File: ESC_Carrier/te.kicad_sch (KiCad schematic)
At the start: 1 part, among them J1 TE 8-5530843-3

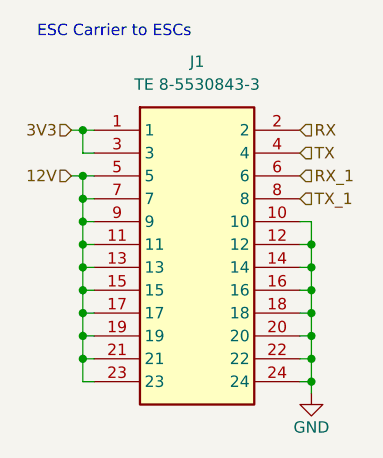
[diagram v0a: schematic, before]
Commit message: Fix: updated esc carrier to esc connectors
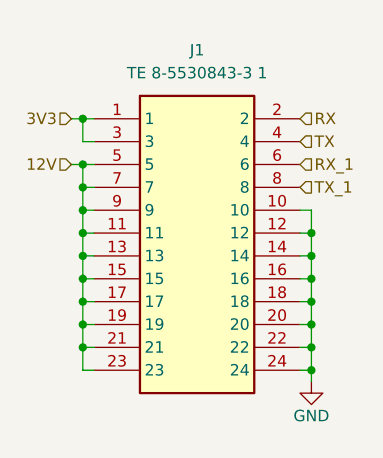
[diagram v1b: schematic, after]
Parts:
- J1: value TE 8-5530843-3 -> TE 8-5530843-3 1; footprint 855308433 -> 8-5530843-3:8-5530843-3
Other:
- note removed: "ESC Carrier to ESCs"

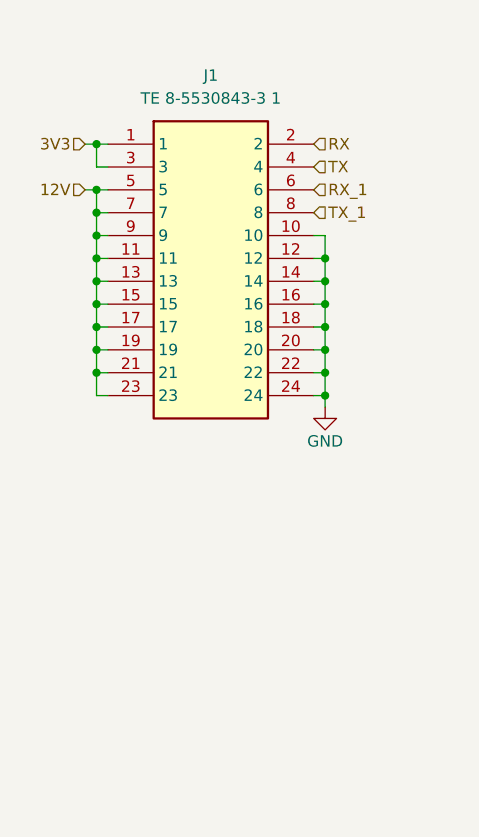
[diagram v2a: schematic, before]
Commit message: Fix: added phases to esc to esc carrier connector
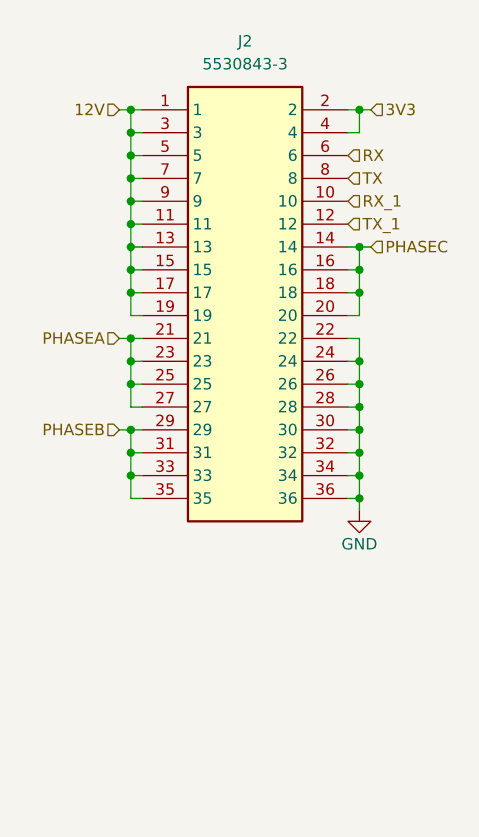
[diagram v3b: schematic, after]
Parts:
- removed J1: TE 8-5530843-3 1, 8-5530843-3:8-5530843-3, symbol 8-5530843-3:8-5530843-3
- added J2: 5530843-3, RHDR36W89P485X254_2X18_5232X928X1549P, symbol 5530843-3:5530843-3
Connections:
- net 12V: now also J2.1, J2.11, J2.13, J2.15, J2.17, J2.19, J2.3, J2.5, J2.7, J2.9
- net 3V3: now also J2.2, J2.4
- net GND: now also J2.22, J2.24, J2.26, J2.28, J2.30, J2.32, J2.34, J2.36
- net RX: now also J2.6
- net RX_1: now also J2.10
- net TX: now also J2.8
- net TX_1: now also J2.12
- new net PHASEA: J2.21, J2.23, J2.25, J2.27
- new net PHASEB: J2.29, J2.31, J2.33, J2.35
- new net PHASEC: J2.14, J2.16, J2.18, J2.20

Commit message: Feat: updated esc to esc carrier connector, updated test points
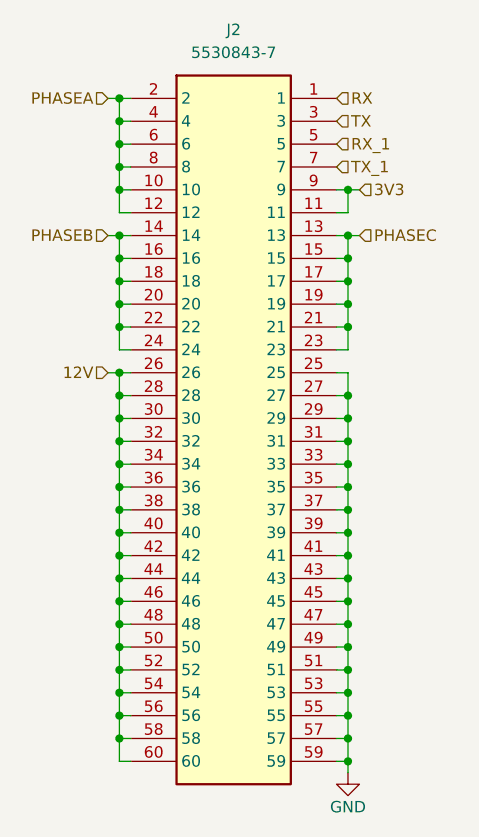
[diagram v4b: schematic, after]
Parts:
- removed J2: 5530843-3, RHDR36W89P485X254_2X18_5232X928X1549P, symbol 5530843-3:5530843-3
- added J2: 5530843-7, 55308437, symbol 5530843-7:5530843-7
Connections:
- net 12V: now also J2.26, J2.28, J2.30, J2.32, J2.34, J2.36, J2.38, J2.40, J2.42, J2.44, J2.46, J2.48, J2.50, J2.52, J2.54, J2.56, J2.58, J2.60
- net 3V3: now also J2.11, J2.9
- net GND: now also J2.25, J2.27, J2.29, J2.31, J2.33, J2.35, J2.37, J2.39, J2.41, J2.43, J2.45, J2.47, J2.49, J2.51, J2.53, J2.55, J2.57, J2.59
- net PHASEA: now also J2.10, J2.12, J2.2, J2.4, J2.6, J2.8
- net PHASEB: now also J2.14, J2.16, J2.18, J2.20, J2.22, J2.24
- net PHASEC: now also J2.13, J2.15, J2.17, J2.19, J2.21, J2.23
- net RX: now also J2.1
- net RX_1: now also J2.5
- net TX: now also J2.3
- net TX_1: now also J2.7

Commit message: Feat: initial placement of components
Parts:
- J2: footprint 55308437 -> 5530843-7:55308437
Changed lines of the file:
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@@
       (effects (font (size 1.27 1.27)))
     )
-    (property "Footprint" "55308437" (at 44.45 116.51 0)
+    (property "Footprint" "5530843-7:55308437" (at 44.45 116.51 0)
       (effects (font (size 1.27 1.27)) (justify left top) hide)
     )

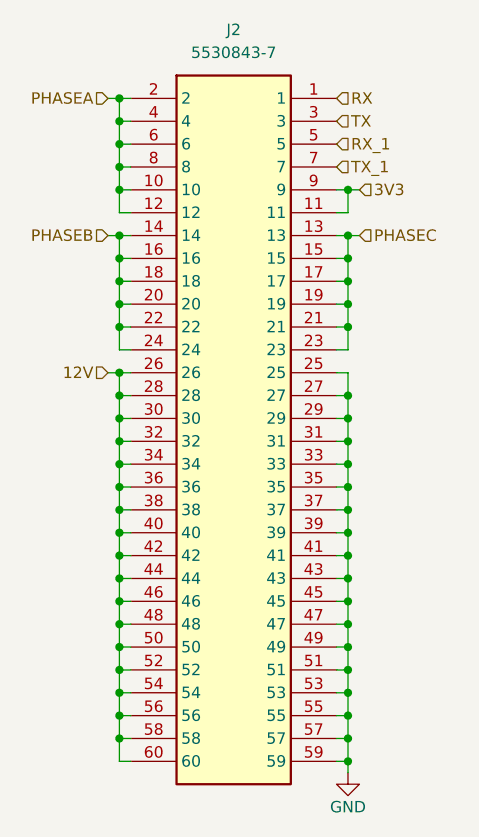
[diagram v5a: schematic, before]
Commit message: Feat: added some traces between components
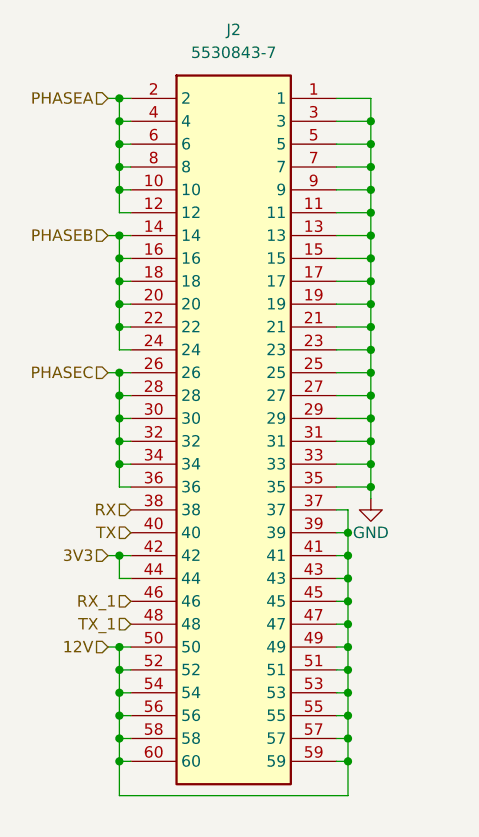
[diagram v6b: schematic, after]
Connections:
- net 12V: now also J2.37, J2.39, J2.41, J2.43, J2.45, J2.47, J2.49, J2.51, J2.53, J2.55, J2.57, J2.59; no longer J2.26, J2.28, J2.30, J2.32, J2.34, J2.36, J2.38, J2.40, J2.42, J2.44, J2.46, J2.48
- net 3V3: now also J2.42, J2.44; no longer J2.11, J2.9
- net GND: now also J2.1, J2.11, J2.13, J2.15, J2.17, J2.19, J2.21, J2.23, J2.3, J2.5, J2.7, J2.9; no longer J2.37, J2.39, J2.41, J2.43, J2.45, J2.47, J2.49, J2.51, J2.53, J2.55, J2.57, J2.59
- net PHASEC: now also J2.26, J2.28, J2.30, J2.32, J2.34, J2.36; no longer J2.13, J2.15, J2.17, J2.19, J2.21, J2.23
- net RX: now also J2.38; no longer J2.1
- net RX_1: now also J2.46; no longer J2.5
- net TX: now also J2.40; no longer J2.3
- net TX_1: now also J2.48; no longer J2.7

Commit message: Feat: added routes and copper fill zones (phases not done)
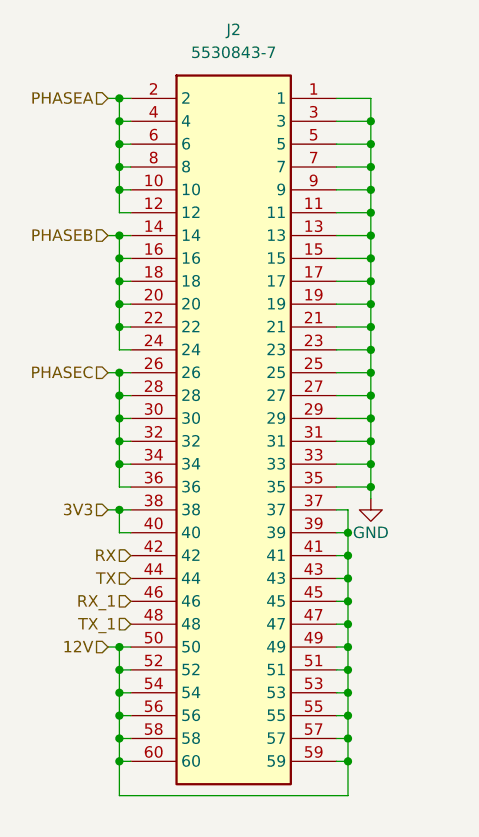
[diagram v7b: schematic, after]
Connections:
- net 3V3: now also J2.38, J2.40; no longer J2.42, J2.44
- net RX: now also J2.42; no longer J2.38
- net TX: now also J2.44; no longer J2.40
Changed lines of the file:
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@@
   (junction (at 24.13 87.63) (diameter 0) (color 0 0 0 0)
   )
+  (junction (at 24.13 67.31) (diameter 0) (color 0 0 0 0)
+  )
   (junction (at 49.53 69.85) (diameter 0) (color 0 0 0 0)
   )
@@
   (junction (at 52.07 54.61) (diameter 0) (color 0 0 0 0)
   )
-  (junction (at 24.13 72.39) (diameter 0) (color 0 0 0 0)
-  )
   (junction (at 24.13 29.21) (diameter 0) (color 0 0 0 0)
   )
@@
     (stroke (width 0) (type default))
   )
+  (wire (pts (xy 25.4 67.31) (xy 24.13 67.31))
+    (stroke (width 0) (type default))
+  )
   (wire (pts (xy 24.13 29.21) (xy 24.13 31.75))
     (stroke (width 0) (type default))
@@
     (stroke (width 0) (type default))
   )
-  (wire (pts (xy 24.13 74.93) (xy 25.4 74.93))
-    (stroke (width 0) (type default))
-  )
   (wire (pts (xy 49.53 74.93) (xy 49.53 72.39))
     (stroke (width 0) (type default))
@@
     (stroke (width 0) (type default))
   )
-  (wire (pts (xy 24.13 72.39) (xy 24.13 74.93))
-    (stroke (width 0) (type default))
-  )
   (wire (pts (xy 48.26 59.69) (xy 52.07 59.69))
     (stroke (width 0) (type default))
@@
     (stroke (width 0) (type default))
   )
+  (wire (pts (xy 24.13 67.31) (xy 24.13 69.85))
+    (stroke (width 0) (type default))
+  )
   (wire (pts (xy 48.26 74.93) (xy 49.53 74.93))
     (stroke (width 0) (type default))
@@
     (stroke (width 0) (type default))
   )
+  (wire (pts (xy 24.13 69.85) (xy 25.4 69.85))
+    (stroke (width 0) (type default))
+  )
   (wire (pts (xy 24.13 31.75) (xy 24.13 34.29))
     (stroke (width 0) (type default))
@@
     (stroke (width 0) (type default))
   )
-  (wire (pts (xy 22.86 72.39) (xy 24.13 72.39))
-    (stroke (width 0) (type default))
-  )
   (wire (pts (xy 48.26 39.37) (xy 52.07 39.37))
     (stroke (width 0) (type default))
@@
     (stroke (width 0) (type default))
   )
+  (wire (pts (xy 22.86 67.31) (xy 24.13 67.31))
+    (stroke (width 0) (type default))
+  )
   (wire (pts (xy 22.86 36.83) (xy 24.13 36.83))
     (stroke (width 0) (type default))
@@
     (stroke (width 0) (type default))
   )
-  (wire (pts (xy 25.4 72.39) (xy 24.13 72.39))
-    (stroke (width 0) (type default))
-  )
   (wire (pts (xy 25.4 52.07) (xy 24.13 52.07))
     (stroke (width 0) (type default))
@@
     (stroke (width 0) (type default))
   )
-  (hierarchical_label "TX" (shape input) (at 25.4 69.85 180) (fields_autoplaced)
-    (effects (font (size 1.27 1.27)) (justify right))
-  )
   (hierarchical_label "PHASEA" (shape input) (at 22.86 21.59 180) (fields_autoplaced)
     (effects (font (size 1.27 1.27)) (justify right))
   )
+  (hierarchical_label "RX" (shape input) (at 25.4 72.39 180) (fields_autoplaced)
+    (effects (font (size 1.27 1.27)) (justify right))
+  )
+  (hierarchical_label "PHASEC" (shape input) (at 22.86 52.07 180) (fields_autoplaced)
+    (effects (font (size 1.27 1.27)) (justify right))
+  )
   (hierarchical_label "TX_1" (shape input) (at 25.4 80.01 180) (fields_autoplaced)
     (effects (font (size 1.27 1.27)) (justify right))
   )
-  (hierarchical_label "PHASEC" (shape input) (at 22.86 52.07 180) (fields_autoplaced)
-    (effects (font (size 1.27 1.27)) (justify right))
-  )
   (hierarchical_label "12V" (shape input) (at 22.86 82.55 180) (fields_autoplaced)
     (effects (font (size 1.27 1.27)) (justify right))
   )
+  (hierarchical_label "PHASEB" (shape input) (at 22.86 36.83 180) (fields_autoplaced)
+    (effects (font (size 1.27 1.27)) (justify right))
+  )
   (hierarchical_label "RX_1" (shape input) (at 25.4 77.47 180) (fields_autoplaced)
     (effects (font (size 1.27 1.27)) (justify right))
   )
-  (hierarchical_label "PHASEB" (shape input) (at 22.86 36.83 180) (fields_autoplaced)
-    (effects (font (size 1.27 1.27)) (justify right))
-  )
-  (hierarchical_label "RX" (shape input) (at 25.4 67.31 180) (fields_autoplaced)
-    (effects (font (size 1.27 1.27)) (justify right))
-  )
-  (hierarchical_label "3V3" (shape input) (at 22.86 72.39 180) (fields_autoplaced)
-    (effects (font (size 1.27 1.27)) (justify right))
-  )
+  (hierarchical_label "TX" (shape input) (at 25.4 74.93 180) (fields_autoplaced)
+    (effects (font (size 1.27 1.27)) (justify right))
+  )
+  (hierarchical_label "3V3" (shape input) (at 22.86 67.31 180) (fields_autoplaced)
+    (effects (font (size 1.27 1.27)) (justify right))
+  )

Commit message: Feat: switched phase connector to microfit, updated esc connector pinout, updated component layout
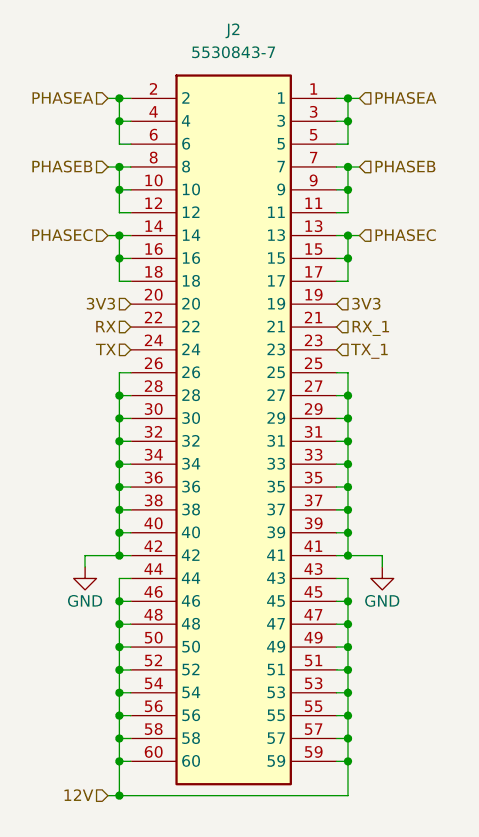
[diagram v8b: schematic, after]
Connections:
- net 12V: now also J2.44, J2.46, J2.48; no longer J2.37, J2.39, J2.41
- net 3V3: now also J2.19, J2.20; no longer J2.38, J2.40
- net GND: now also J2.26, J2.28, J2.30, J2.32, J2.34, J2.36, J2.37, J2.38, J2.39, J2.40, J2.41, J2.42; no longer J2.1, J2.11, J2.13, J2.15, J2.17, J2.19, J2.21, J2.23, J2.3, J2.5, J2.7, J2.9
- net PHASEA: now also J2.1, J2.3, J2.5; no longer J2.10, J2.12, J2.8
- net PHASEB: now also J2.10, J2.11, J2.12, J2.7, J2.8, J2.9; no longer J2.14, J2.16, J2.18, J2.20, J2.22, J2.24
- net PHASEC: now also J2.13, J2.14, J2.15, J2.16, J2.17, J2.18; no longer J2.26, J2.28, J2.30, J2.32, J2.34, J2.36
- net RX: now also J2.22; no longer J2.42
- net RX_1: now also J2.21; no longer J2.46
- net TX: now also J2.24; no longer J2.44
- net TX_1: now also J2.23; no longer J2.48
